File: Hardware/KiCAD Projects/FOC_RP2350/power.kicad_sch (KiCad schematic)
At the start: 24 parts, among them J401 GT-USB-7025, J402 DB125-2.54-6P-GN-S, J403 MKS Power, J404 XT30U-M, J405 ZX-PZ2.54-2-6PZZ, J406 PZ254-1-13-Z-8.5, J407 PZ254-1-13-Z-8.5, Q401 AO3401A, U401 AMS1117-3.3, U402 ACS711KLCTR-25AB-T, U403 TSR1-2450E, U404 TSR1-2433E

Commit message: Hardware update
- Removed 5V net as it is not really needed for typical SimpleFOC encoders. This reduces part cost a lot.
- Fixed SPI pin assignment
- Exposed another GPIO pin in place of the +5V pin
- Boards changed to transfer power via the standoff pads instead of a solder connection
- Moved accelerometer to the controller board
- Resistance changes to reduce BOM
- Replaced encoder connection with JST-XH
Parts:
- removed D401, D402: KT-0805G, LED_SMD:LED_0805_2012Metric, symbol Device:LED
- removed J403: MKS Power, TestPoint:TestPoint_2Pads_Pitch5.08mm_Drill1.3mm, symbol Connector:Conn_01x02_Pin
- removed J405: ZX-PZ2.54-2-6PZZ, Connector_PinHeader_2.54mm:PinHeader_2x06_P2.54mm_Vertical, symbol Connector_Generic:Conn_02x06_Odd_Even
- removed Q401: AO3401A, Package_TO_SOT_SMD:SOT-23, symbol Transistor_FET:AO3401A
- removed R405: 1k, Resistor_SMD:R_0805_2012Metric, symbol Device:R
- removed R406: 680, Resistor_SMD:R_0805_2012Metric, symbol Device:R
- removed U404: TSR1-2433E, Converter_DCDC:Converter_DCDC_TRACO_TSR1-xxxxE_THT, symbol Converter_DCDC:TSR1-2433E
- added D401: SS12, Diode_SMD:D_SMA, symbol Diode:SS12
- added H401, H402, H403, H404: MountingHole_Pad, MountingHole:MountingHole_3.2mm_M3_Pad_Via, symbol Mechanical:MountingHole_Pad
- added J403, J408: Conn_01x05, Connector_JST:JST_XH_B5B-XH-A_1x05_P2.50mm_Vertical, symbol Connector_Generic:Conn_01x05
- U403: value TSR1-2450E -> TSR1-2433E
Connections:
- net 3V3: now also U403.3 (Vout), J403.1 (Pin_1), J408.1 (Pin_1)
- net GND: now also H403.1, H404.1, J403.5 (Pin_5), J408.5 (Pin_5)
- net Mot0_EncA: now also J403.2 (Pin_2)
- net Mot0_EncB: now also J403.3 (Pin_3)
- net Mot0_EncI: now also J403.4 (Pin_4)
- net Mot1_EncA: now also J408.2 (Pin_2)
- net Mot1_EncB: now also J408.3 (Pin_3)
- net Mot1_EncI: now also J408.4 (Pin_4)
- net VCON: now also D401.2 (A)
- net VMOT: now also H401.1, H402.1; no longer U403.1 (Vin)
- net 5V renamed Shield_Res112
- new net: D401.1 (K), U403.1 (Vin)
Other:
- note added: "Input Sensing"
- note added: "USB & 3.3V Regulators"
- note removed: "3.3V from Motor Supply"
- note removed: "3.3V from USB"
- note removed: "5V from Motor Supply"
- moved on the sheet: C401, C402, C403, F401, J401, J402, J404, R401, R402, R403, R404, U401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

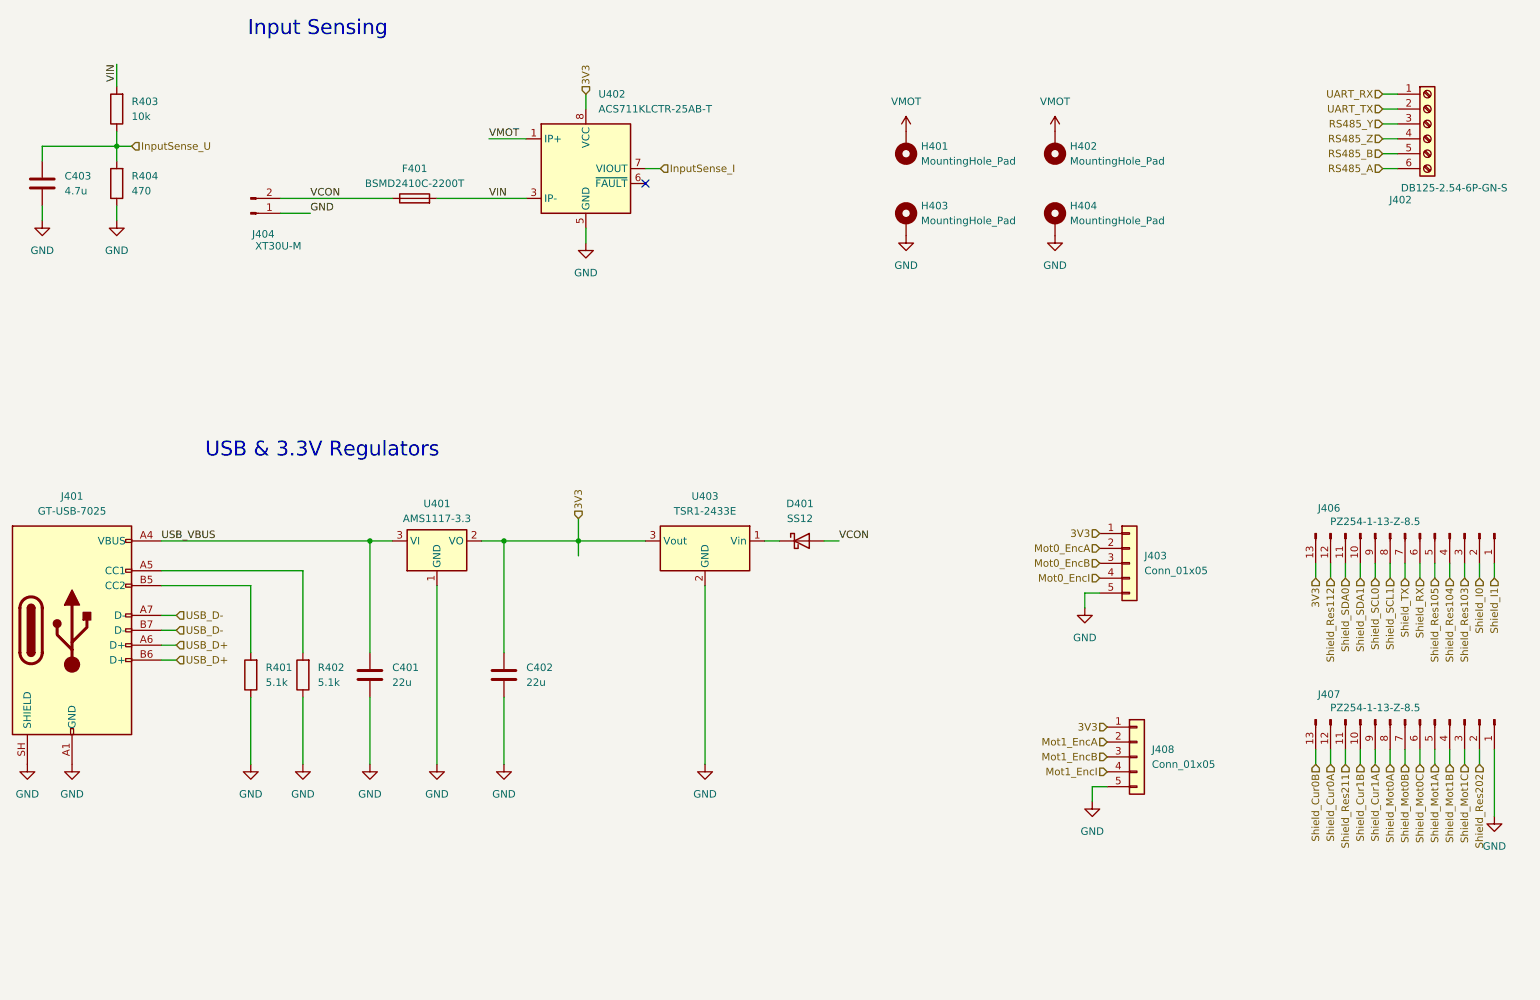
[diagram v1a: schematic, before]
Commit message: Driver redesign to allow 8323H and 8323S
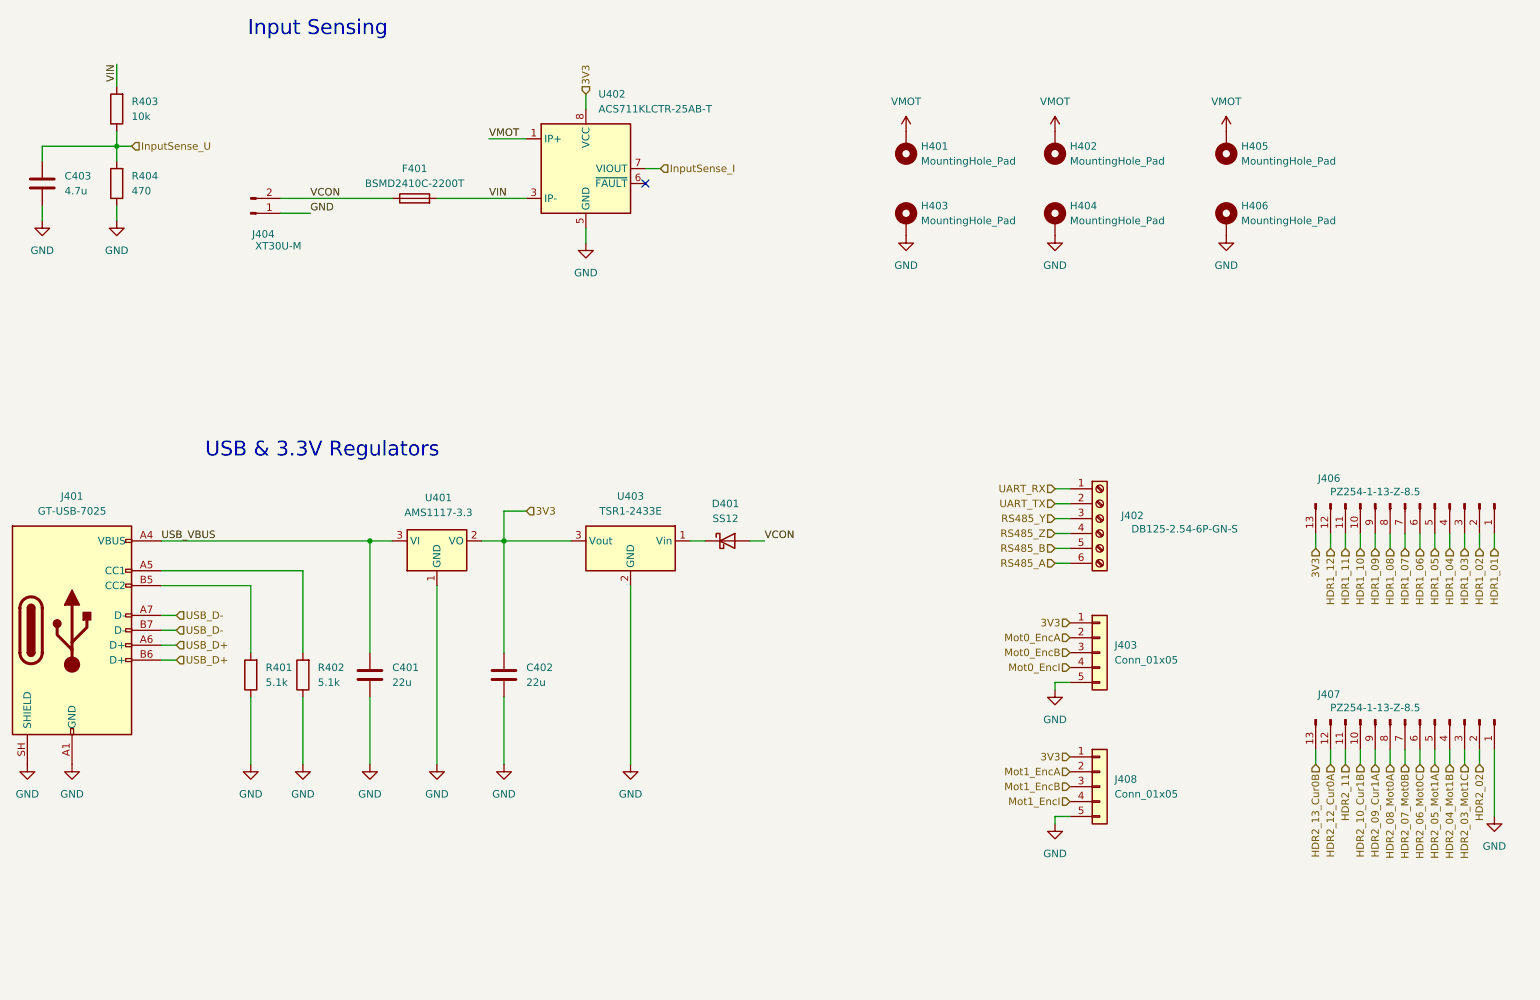
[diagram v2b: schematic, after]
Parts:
- added H405, H406: MountingHole_Pad, TestPoint:TestPoint_THTPad_D2.0mm_Drill1.0mm, symbol Mechanical:MountingHole_Pad
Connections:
- net GND: now also H406.1
- net VMOT: now also H405.1
- net Shield_Cur0A renamed HDR2_12_Cur0A
- net Shield_Cur0B renamed HDR2_13_Cur0B
- net Shield_Cur1A renamed HDR2_09_Cur1A
- net Shield_Cur1B renamed HDR2_10_Cur1B
- net Shield_I0 renamed HDR1_02
- net Shield_I1 renamed HDR1_01
- net Shield_Mot0A renamed HDR2_08_Mot0A
- net Shield_Mot0B renamed HDR2_07_Mot0B
- net Shield_Mot0C renamed HDR2_06_Mot0C
- net Shield_Mot1A renamed HDR2_05_Mot1A
- net Shield_Mot1B renamed HDR2_04_Mot1B
- net Shield_Mot1C renamed HDR2_03_Mot1C
- net Shield_RX renamed HDR1_06
- net Shield_Res103 renamed HDR1_03
- net Shield_Res104 renamed HDR1_04
- net Shield_Res105 renamed HDR1_05
- net Shield_Res112 renamed HDR1_12
- net Shield_Res202 renamed HDR2_02
- net Shield_Res211 renamed HDR2_11
- net Shield_SCL0 renamed HDR1_09
- net Shield_SCL1 renamed HDR1_08
- net Shield_SDA0 renamed HDR1_11
- net Shield_SDA1 renamed HDR1_10
- net Shield_TX renamed HDR1_07
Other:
- moved on the sheet: D401, J402, J403, J406, J408, U403
